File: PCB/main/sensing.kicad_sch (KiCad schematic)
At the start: 4 parts

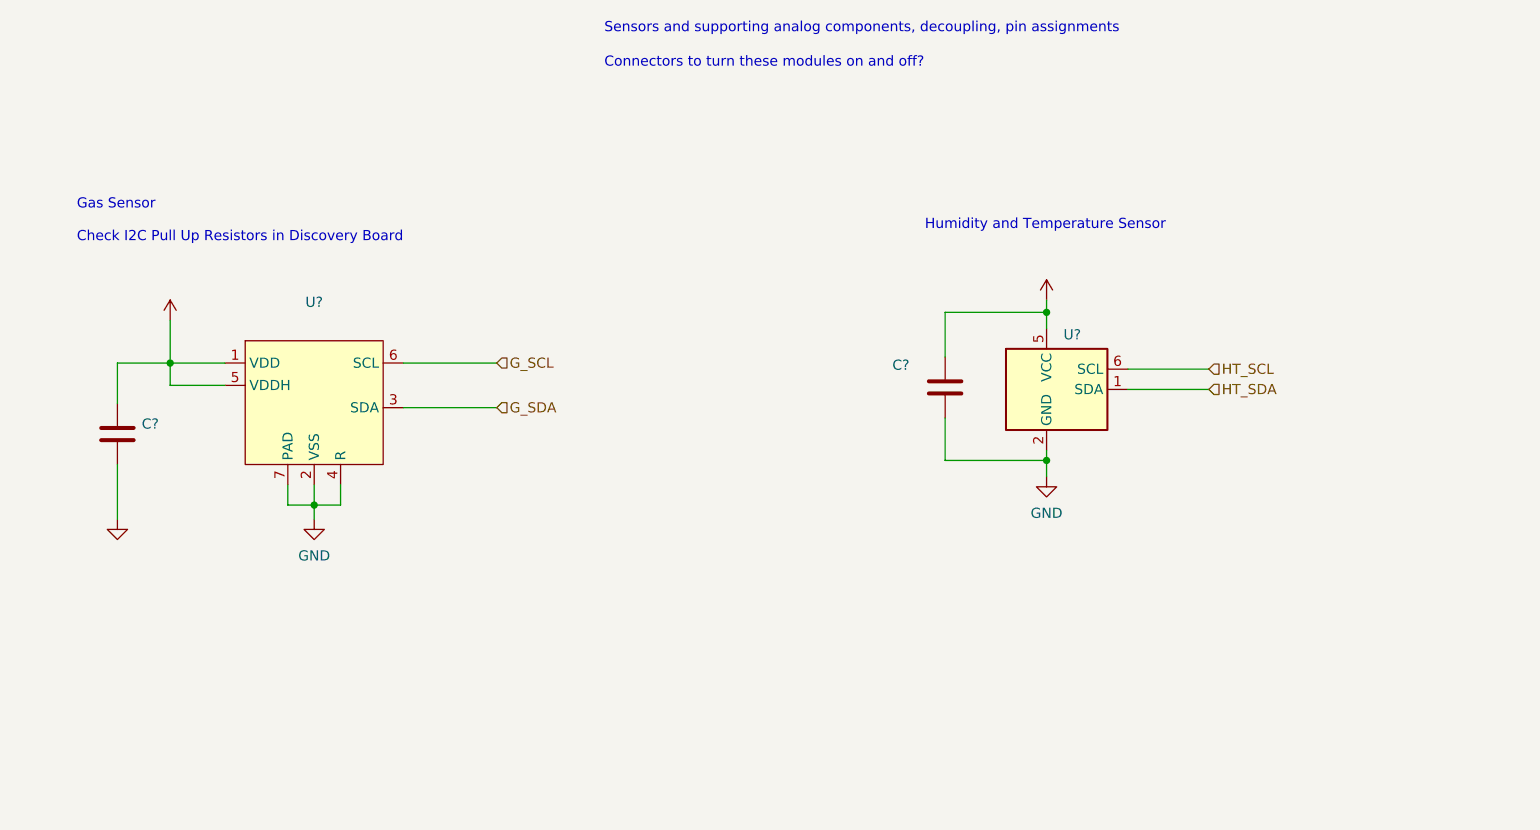
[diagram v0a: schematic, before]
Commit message: added eeprom and some usb-uart connections
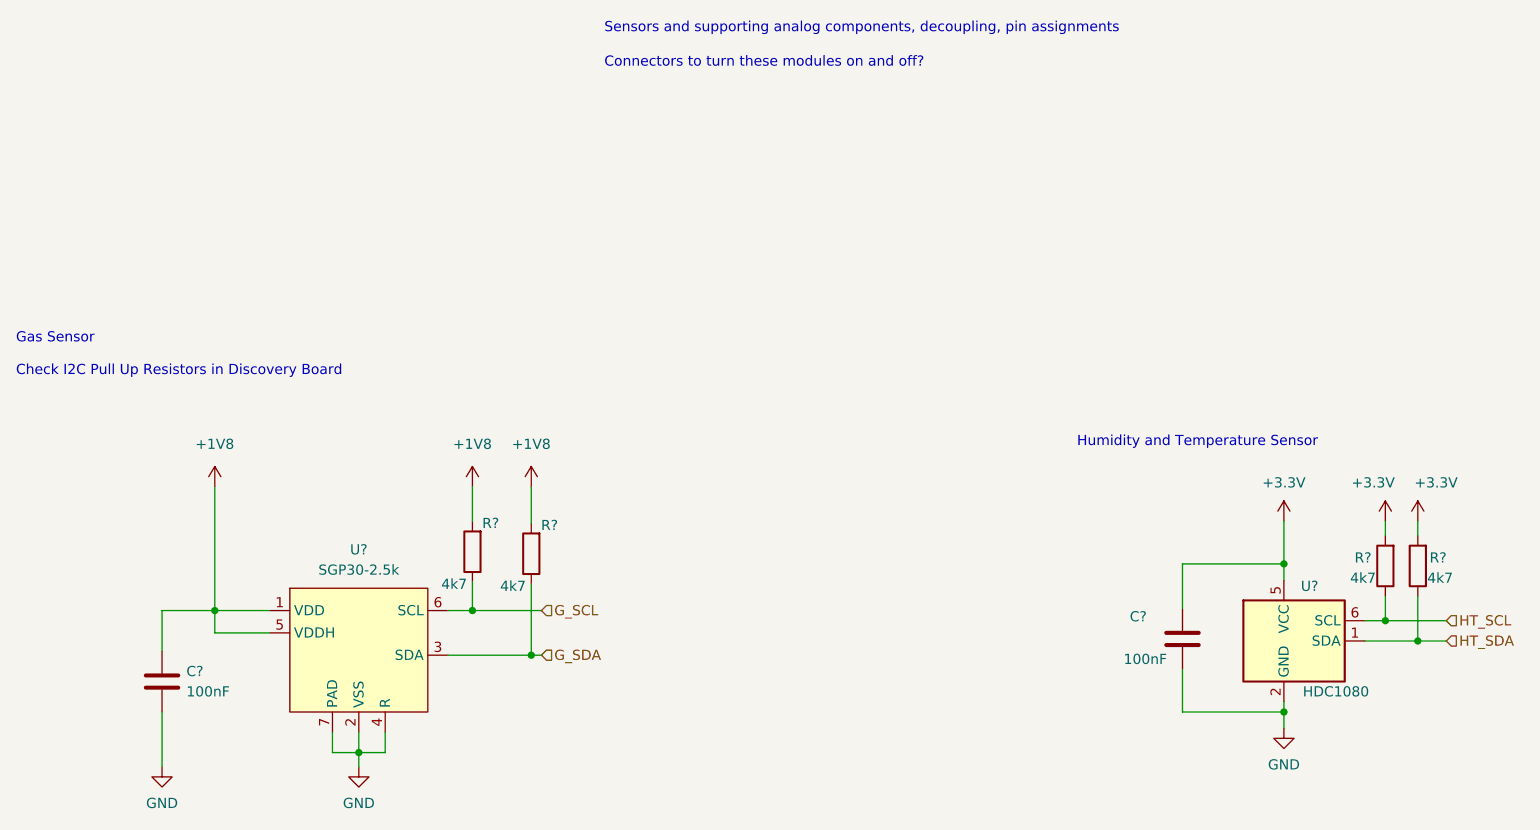
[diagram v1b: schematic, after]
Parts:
- added R? (x4): 4k7, Resistor_SMD:R_0603_1608Metric_Pad0.98x0.95mm_HandSolder, symbol Device:R
- C? (x2): value (none) -> 100nF; footprint (none) -> Capacitor_SMD:C_0603_1608Metric_Pad1.08x0.95mm_HandSolder
- U?: value (none) -> HDC1080; footprint (none) -> Package_SON:Texas_PWSON-N6
- U?: value (none) -> SGP30-2.5k; footprint (none) -> LIB_SGPC3-2:SON80P245X245X90-7N
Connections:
- net +1V8: now also R?.2, R?.2
- net +3V3: now also R?.2, R?.2
- net G_SCL: now also R?.1
- net G_SDA: now also R?.1
- net HT_SCL: now also R?.1
- net HT_SDA: now also R?.1
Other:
- moved on the sheet: C?, U?

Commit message: added ESD protection and updated USB IC
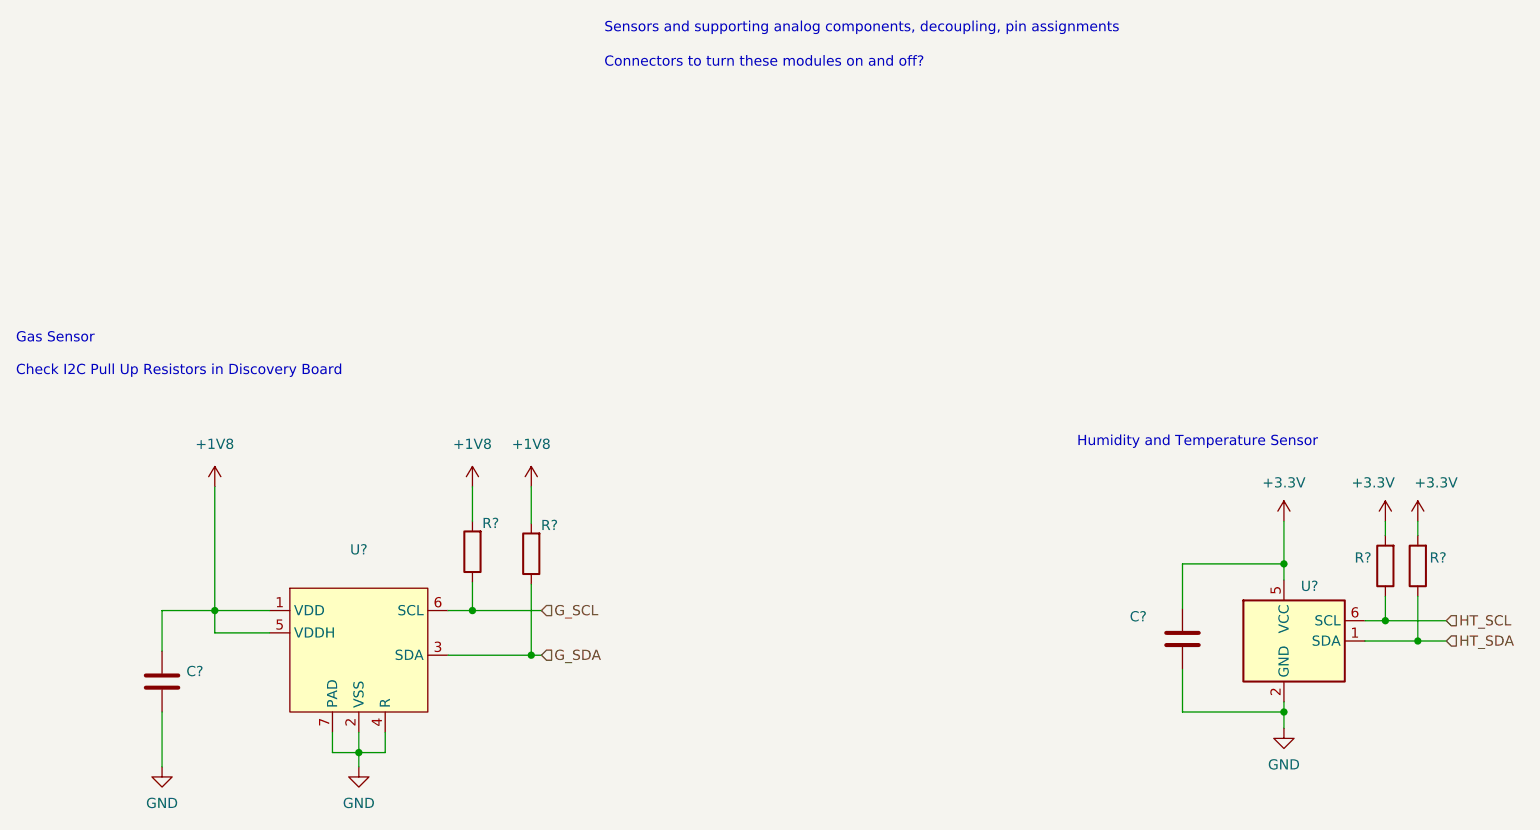
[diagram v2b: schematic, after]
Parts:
- C? (x2): value 100nF -> (none); footprint Capacitor_SMD:C_0603_1608Metric_Pad1.08x0.95mm_HandSolder -> (none); Price (none) -> $0.0026
- R? (x4): value 4k7 -> (none); footprint Resistor_SMD:R_0603_1608Metric_Pad0.98x0.95mm_HandSolder -> (none)
- U?: value HDC1080 -> (none); footprint Package_SON:Texas_PWSON-N6 -> (none)
- U?: value SGP30-2.5k -> (none); footprint LIB_SGPC3-2:SON80P245X245X90-7N -> (none)
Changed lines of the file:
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@@
       (effects (font (size 1.27 1.27)) (justify right))
     )
-    (property "Value" "HDC1080" (id 1) (at 214.376 99.822 0)
+    (property "Value" "" (id 1) (at 214.376 99.822 0)
       (effects (font (size 1.27 1.27)) (justify right))
     )
-    (property "Footprint" "Package_SON:Texas_PWSON-N6" (id 2) (at 204.978 99.822 0)
+    (property "Footprint" "" (id 2) (at 204.978 99.822 0)
       (effects (font (size 1.27 1.27)) (justify left) hide)
     )
@@
     (in_bom yes) (on_board yes)
     (property "Reference" "R?" (id 0) (at 213.614 83.058 0))
-    (property "Value" "4k7" (id 1) (at 213.614 85.598 0))
-    (property "Footprint" "Resistor_SMD:R_0603_1608Metric_Pad0.98x0.95mm_HandSolder" (id 2) (at 218.186 84.074 90)
+    (property "Value" "" (id 1) (at 213.614 85.598 0))
+    (property "Footprint" "" (id 2) (at 218.186 84.074 90)
       (effects (font (size 1.27 1.27)) hide)
     )
@@
     (in_bom yes) (on_board yes)
     (property "Reference" "R?" (id 0) (at 223.012 83.058 0))
-    (property "Value" "4k7" (id 1) (at 223.266 85.598 0))
-    (property "Footprint" "Resistor_SMD:R_0603_1608Metric_Pad0.98x0.95mm_HandSolder" (id 2) (at 222.25 84.074 90)
+    (property "Value" "" (id 1) (at 223.266 85.598 0))
+    (property "Footprint" "" (id 2) (at 222.25 84.074 90)
       (effects (font (size 1.27 1.27)) hide)
     )
@@
       (effects (font (size 1.27 1.27)) (justify left))
     )
-    (property "Value" "100nF" (id 1) (at 66.294 99.8219 0)
-      (effects (font (size 1.27 1.27)) (justify left))
-    )
-    (property "Footprint" "Capacitor_SMD:C_0603_1608Metric_Pad1.08x0.95mm_HandSolder" (id 2) (at 64.2112 102.362 0)
+    (property "Value" "" (id 1) (at 66.294 99.8219 0)
+      (effects (font (size 1.27 1.27)) (justify left))
+    )
+    (property "Footprint" "" (id 2) (at 64.2112 102.362 0)
       (effects (font (size 1.27 1.27)) hide)
     )
@@
     )
     (property "LCSC" "C14663" (id 4) (at 63.246 98.552 0)
+      (effects (font (size 1.27 1.27)) hide)
+    )
+    (property "Price" "$0.0026" (id 5) (at 63.246 98.552 0)
       (effects (font (size 1.27 1.27)) hide)
     )
@@
     (in_bom yes) (on_board yes)
     (property "Reference" "R?" (id 0) (at 111.76 78.994 0))
-    (property "Value" "4k7" (id 1) (at 107.188 86.614 0))
-    (property "Footprint" "Resistor_SMD:R_0603_1608Metric_Pad0.98x0.95mm_HandSolder" (id 2) (at 111.252 82.55 90)
+    (property "Value" "" (id 1) (at 107.188 86.614 0))
+    (property "Footprint" "" (id 2) (at 111.252 82.55 90)
       (effects (font (size 1.27 1.27)) hide)
     )
@@
     (in_bom yes) (on_board yes) (fields_autoplaced)
     (property "Reference" "U?" (id 0) (at 87.884 82.042 0))
-    (property "Value" "SGP30-2.5k" (id 1) (at 87.884 84.582 0))
-    (property "Footprint" "LIB_SGPC3-2:SON80P245X245X90-7N" (id 2) (at 87.63 84.074 0)
+    (property "Value" "" (id 1) (at 87.884 84.582 0))
+    (property "Footprint" "" (id 2) (at 87.63 84.074 0)
       (effects (font (size 1.27 1.27)) hide)
     )
@@
       (effects (font (size 1.27 1.27)) (justify left))
     )
-    (property "Value" "100nF" (id 1) (at 183.642 95.758 0)
-      (effects (font (size 1.27 1.27)) (justify left))
-    )
-    (property "Footprint" "Capacitor_SMD:C_0603_1608Metric_Pad1.08x0.95mm_HandSolder" (id 2) (at 191.9732 97.028 0)
+    (property "Value" "" (id 1) (at 183.642 95.758 0)
+      (effects (font (size 1.27 1.27)) (justify left))
+    )
+    (property "Footprint" "" (id 2) (at 191.9732 97.028 0)
       (effects (font (size 1.27 1.27)) hide)
     )
@@
     )
     (property "LCSC" "C14663" (id 4) (at 191.008 93.218 0)
+      (effects (font (size 1.27 1.27)) hide)
+    )
+    (property "Price" "$0.0026" (id 5) (at 191.008 93.218 0)
       (effects (font (size 1.27 1.27)) hide)
     )
@@
     (in_bom yes) (on_board yes)
     (property "Reference" "R?" (id 0) (at 104.394 78.74 0))
-    (property "Value" "4k7" (id 1) (at 99.822 86.36 0))
-    (property "Footprint" "Resistor_SMD:R_0603_1608Metric_Pad0.98x0.95mm_HandSolder" (id 2) (at 103.886 82.296 90)
-      (effects (font (size 1.27 1.27)) hide)
-    )
+    (property "Value" "" (id 1) (at 99.822 86.36 0))
+    (property "Footprint" "" (id 2) (at 103.886 82.296 90)
+      (effects (font (size 1.27 1.27)) hide)
+    )

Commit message: layout started
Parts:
- removed R? (x2): (no value), symbol Device:R
- added J10, J9: Conn_01x02_Male, Connector_PinHeader_2.54mm:PinHeader_1x02_P2.54mm_Vertical, symbol Connector:Conn_01x02_Male
- added R20: 4k7, Resistor_SMD:R_0603_1608Metric_Pad0.98x0.95mm_HandSolder, symbol Device:R
- added TP10: GAS_SCL, symbol Connector:TestPoint_Alt
- added TP9: GAS_SDA, symbol Connector:TestPoint_Alt
- added U7: TXS0102DCT, Package_SO:SSOP-8_2.95x2.8mm_P0.65mm, symbol Logic_LevelTranslator:TXS0102DCT
- C12, C13: renamed from C?; value (none) -> 100nF; footprint (none) -> Capacitor_SMD:C_0603_1608Metric_Pad1.08x0.95mm_HandSolder
- R22, R23: renamed from R?; value (none) -> 4k7; footprint (none) -> Resistor_SMD:R_0603_1608Metric_Pad0.98x0.95mm_HandSolder
- U5: renamed from U?; value (none) -> SGP30-2.5k; footprint (none) -> LIB_SGPC3-2:SON80P245X245X90-7N
- U6: renamed from U?; value (none) -> HDC1080; footprint (none) -> Package_SON:Texas_PWSON-N6
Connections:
- net +1V8: now also J9.1 (Pin_1), U7.3 (VCCA); no longer C12.1, U5.1 (VDD), U5.5 (VDDH)
- net GND: now also R20.1, U7.2 (GND)
- net G_SCL: now also U7.8 (B1); no longer U5.6 (SCL)
- net G_SDA: now also U7.1 (B2); no longer U5.3 (SDA)
- net +3V3: no longer names the net of C13.1, U6.5 (VCC)
- net +3V3: now also J10.2 (Pin_2); no longer R22.2, R23.2
- new net: R20.2, U7.6 (OE)
- new net: TP10.1, U5.6 (SCL), U7.5 (A1)
- new net: C12.1, J9.2 (Pin_2), U5.1 (VDD), U5.5 (VDDH)
- new net: TP9.1, U5.3 (SDA), U7.4 (A2)
- new net +3V0: J10.1 (Pin_1), R22.2, R23.2, U7.7 (VCCB)
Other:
- note added: "Level Shifter"

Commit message: started on routing
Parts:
- TP10, TP9: footprint (none) -> TestPoint:TestPoint_Pad_D2.0mm
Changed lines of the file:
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@@
       (effects (font (size 1.27 1.27)) (justify left))
     )
-    (property "Footprint" "" (id 2) (at 109.22 88.9 0)
+    (property "Footprint" "TestPoint:TestPoint_Pad_D2.0mm" (id 2) (at 109.22 88.9 0)
       (effects (font (size 1.27 1.27)) hide)
     )
@@
       (effects (font (size 1.27 1.27)) (justify right))
     )
-    (property "Footprint" "" (id 2) (at 96.012 95.25 0)
+    (property "Footprint" "TestPoint:TestPoint_Pad_D2.0mm" (id 2) (at 96.012 95.25 0)
       (effects (font (size 1.27 1.27)) hide)
     )

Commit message: ver 1 complete
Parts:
- C12, C13: value 100nF -> (none); footprint Capacitor_SMD:C_0603_1608Metric_Pad1.08x0.95mm_HandSolder -> (none)
- J10, J9: value Conn_01x02_Male -> (none); footprint Connector_PinHeader_2.54mm:PinHeader_1x02_P2.54mm_Vertical -> (none)
- R20, R22, R23: value 4k7 -> (none); footprint Resistor_SMD:R_0603_1608Metric_Pad0.98x0.95mm_HandSolder -> (none)
- TP10: value GAS_SCL -> (none); footprint TestPoint:TestPoint_Pad_D2.0mm -> (none)
- TP9: value GAS_SDA -> (none); footprint TestPoint:TestPoint_Pad_D2.0mm -> (none)
- U5: value SGP30-2.5k -> (none); footprint LIB_SGPC3-2:SON80P245X245X90-7N -> (none)
- U6: value HDC1080 -> (none); footprint Package_SON:Texas_PWSON-N6 -> (none)
- U7: value TXS0102DCT -> (none); footprint Package_SO:SSOP-8_2.95x2.8mm_P0.65mm -> (none)
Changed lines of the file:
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@@
       (effects (font (size 1.27 1.27)) (justify right))
     )
-    (property "Value" "HDC1080" (id 1) (at 214.376 99.822 0)
+    (property "Value" "" (id 1) (at 214.376 99.822 0)
       (effects (font (size 1.27 1.27)) (justify right))
     )
-    (property "Footprint" "Package_SON:Texas_PWSON-N6" (id 2) (at 204.978 99.822 0)
+    (property "Footprint" "" (id 2) (at 204.978 99.822 0)
       (effects (font (size 1.27 1.27)) (justify left) hide)
     )
@@
     (in_bom yes) (on_board yes)
     (property "Reference" "R22" (id 0) (at 213.614 83.058 0))
-    (property "Value" "4k7" (id 1) (at 213.614 85.598 0))
-    (property "Footprint" "Resistor_SMD:R_0603_1608Metric_Pad0.98x0.95mm_HandSolder" (id 2) (at 218.186 84.074 90)
+    (property "Value" "" (id 1) (at 213.614 85.598 0))
+    (property "Footprint" "" (id 2) (at 218.186 84.074 90)
       (effects (font (size 1.27 1.27)) hide)
     )
@@
     (in_bom yes) (on_board yes)
     (property "Reference" "R20" (id 0) (at 114.3 100.584 0))
-    (property "Value" "4k7" (id 1) (at 114.3 108.204 0))
-    (property "Footprint" "Resistor_SMD:R_0603_1608Metric_Pad0.98x0.95mm_HandSolder" (id 2) (at 118.364 104.14 90)
+    (property "Value" "" (id 1) (at 114.3 108.204 0))
+    (property "Footprint" "" (id 2) (at 118.364 104.14 90)
       (effects (font (size 1.27 1.27)) hide)
     )
@@
       (effects (font (size 1.27 1.27)) (justify left))
     )
-    (property "Value" "GAS_SCL" (id 1) (at 97.79 81.534 0)
-      (effects (font (size 1.27 1.27)) (justify left))
-    )
-    (property "Footprint" "TestPoint:TestPoint_Pad_D2.0mm" (id 2) (at 109.22 88.9 0)
+    (property "Value" "" (id 1) (at 97.79 81.534 0)
+      (effects (font (size 1.27 1.27)) (justify left))
+    )
+    (property "Footprint" "" (id 2) (at 109.22 88.9 0)
       (effects (font (size 1.27 1.27)) hide)
     )
@@
     (in_bom yes) (on_board yes)
     (property "Reference" "J9" (id 0) (at 64.77 77.47 0))
-    (property "Value" "Conn_01x02_Male" (id 1) (at 65.405 76.2 0)
-      (effects (font (size 1.27 1.27)) hide)
-    )
-    (property "Footprint" "Connector_PinHeader_2.54mm:PinHeader_1x02_P2.54mm_Vertical" (id 2) (at 64.77 79.248 0)
+    (property "Value" "" (id 1) (at 65.405 76.2 0)
+      (effects (font (size 1.27 1.27)) hide)
+    )
+    (property "Footprint" "" (id 2) (at 64.77 79.248 0)
       (effects (font (size 1.27 1.27)) hide)
     )
@@
     (in_bom yes) (on_board yes)
     (property "Reference" "J10" (id 0) (at 198.628 77.978 0))
-    (property "Value" "Conn_01x02_Male" (id 1) (at 199.263 76.708 0)
-      (effects (font (size 1.27 1.27)) hide)
-    )
-    (property "Footprint" "Connector_PinHeader_2.54mm:PinHeader_1x02_P2.54mm_Vertical" (id 2) (at 198.628 79.756 0)
+    (property "Value" "" (id 1) (at 199.263 76.708 0)
+      (effects (font (size 1.27 1.27)) hide)
+    )
+    (property "Footprint" "" (id 2) (at 198.628 79.756 0)
       (effects (font (size 1.27 1.27)) hide)
     )
@@
     (in_bom yes) (on_board yes)
     (property "Reference" "R23" (id 0) (at 223.012 83.058 0))
-    (property "Value" "4k7" (id 1) (at 223.266 85.598 0))
-    (property "Footprint" "Resistor_SMD:R_0603_1608Metric_Pad0.98x0.95mm_HandSolder" (id 2) (at 222.25 84.074 90)
+    (property "Value" "" (id 1) (at 223.266 85.598 0))
+    (property "Footprint" "" (id 2) (at 222.25 84.074 90)
       (effects (font (size 1.27 1.27)) hide)
     )
@@
       (effects (font (size 1.27 1.27)) (justify right))
     )
-    (property "Value" "GAS_SDA" (id 1) (at 97.79 100.584 0)
+    (property "Value" "" (id 1) (at 97.79 100.584 0)
       (effects (font (size 1.27 1.27)) (justify right))
     )
-    (property "Footprint" "TestPoint:TestPoint_Pad_D2.0mm" (id 2) (at 96.012 95.25 0)
+    (property "Footprint" "" (id 2) (at 96.012 95.25 0)
       (effects (font (size 1.27 1.27)) hide)
     )
@@
       (effects (font (size 1.27 1.27)) (justify left))
     )
-    (property "Value" "100nF" (id 1) (at 66.294 99.8219 0)
-      (effects (font (size 1.27 1.27)) (justify left))
-    )
-    (property "Footprint" "Capacitor_SMD:C_0603_1608Metric_Pad1.08x0.95mm_HandSolder" (id 2) (at 64.2112 102.362 0)
+    (property "Value" "" (id 1) (at 66.294 99.8219 0)
+      (effects (font (size 1.27 1.27)) (justify left))
+    )
+    (property "Footprint" "" (id 2) (at 64.2112 102.362 0)
       (effects (font (size 1.27 1.27)) hide)
     )
@@
       (effects (font (size 1.27 1.27)) (justify left))
     )
-    (property "Value" "TXS0102DCT" (id 1) (at 131.3054 107.696 0)
-      (effects (font (size 1.27 1.27)) (justify left))
-    )
-    (property "Footprint" "Package_SO:SSOP-8_2.95x2.8mm_P0.65mm" (id 2) (at 129.286 106.68 0)
+    (property "Value" "" (id 1) (at 131.3054 107.696 0)
+      (effects (font (size 1.27 1.27)) (justify left))
+    )
+    (property "Footprint" "" (id 2) (at 129.286 106.68 0)
       (effects (font (size 1.27 1.27)) hide)
     )
@@
     (in_bom yes) (on_board yes) (fields_autoplaced)
     (property "Reference" "U5" (id 0) (at 87.884 82.042 0))
-    (property "Value" "SGP30-2.5k" (id 1) (at 87.884 84.582 0))
-    (property "Footprint" "LIB_SGPC3-2:SON80P245X245X90-7N" (id 2) (at 87.63 84.074 0)
+    (property "Value" "" (id 1) (at 87.884 84.582 0))
+    (property "Footprint" "" (id 2) (at 87.63 84.074 0)
       (effects (font (size 1.27 1.27)) hide)
     )
@@
       (effects (font (size 1.27 1.27)) (justify left))
     )
-    (property "Value" "100nF" (id 1) (at 183.642 95.758 0)
-      (effects (font (size 1.27 1.27)) (justify left))
-    )
-    (property "Footprint" "Capacitor_SMD:C_0603_1608Metric_Pad1.08x0.95mm_HandSolder" (id 2) (at 191.9732 97.028 0)
-      (effects (font (size 1.27 1.27)) hide)
-    )
+    (property "Value" "" (id 1) (at 183.642 95.758 0)
+      (effects (font (size 1.27 1.27)) (justify left))
+    )
+    (property "Footprint" "" (id 2) (at 191.9732 97.028 0)
+      (effects (font (size 1.27 1.27)) hide)
+    )
